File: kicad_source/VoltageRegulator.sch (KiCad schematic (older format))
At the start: 45 parts, among them CN6 691313710002, Q1 IPD90P03P4L- 04, U3 LM1085ISX-ADJ/NOPB, U9 IFX91041EJV

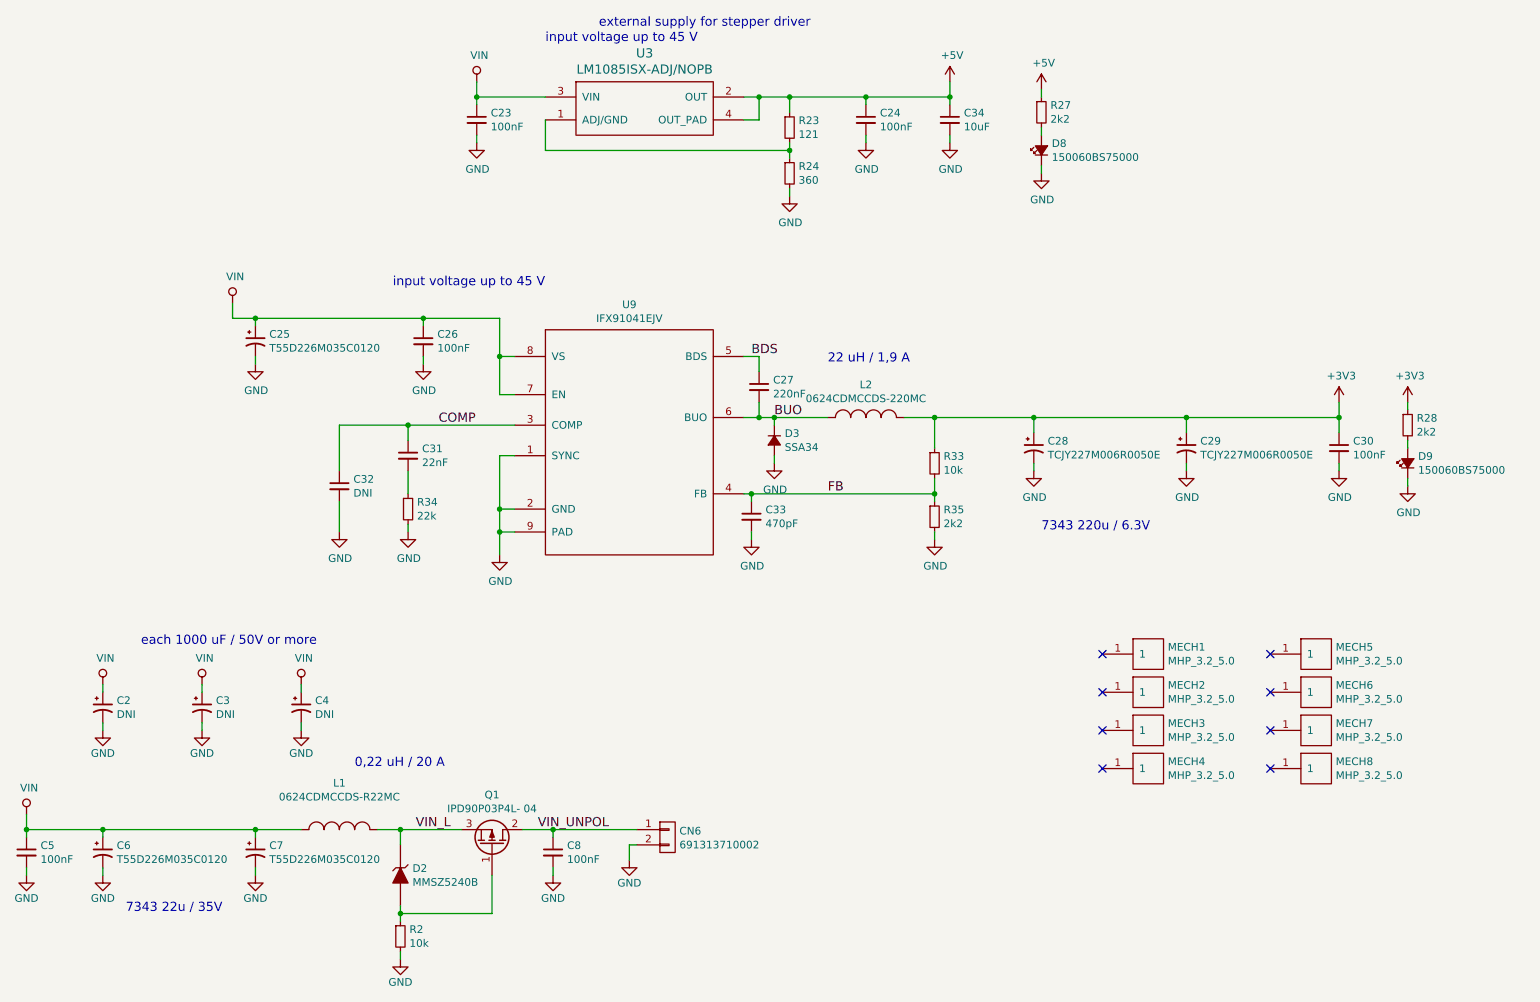
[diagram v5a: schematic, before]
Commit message: removed regulator for 5V external
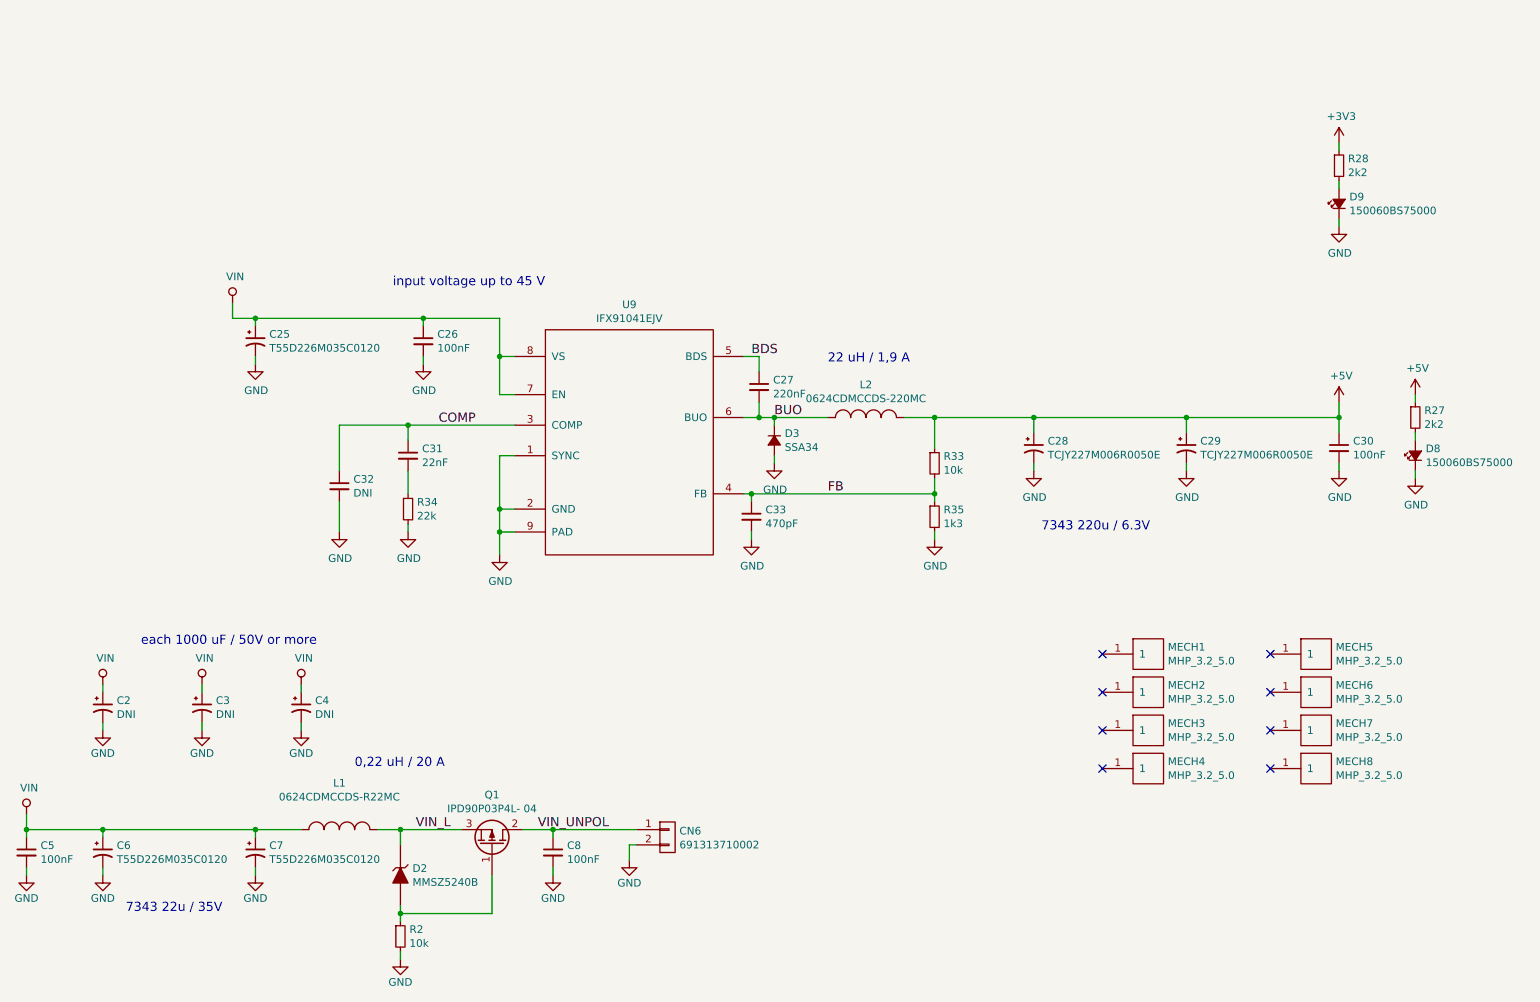
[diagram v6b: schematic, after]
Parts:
- removed C23, C24: 100nF, capacitors:C_0603, symbol devices:C_0603
- removed C34: 10uF, capacitors:C_0805, symbol devices:C_0805
- removed R23: 121, resistors:R_0603, symbol devices:R_0603
- removed R24: 360, resistors:R_0603, symbol devices:R_0603
- removed U3: LM1085ISX-ADJ/NOPB, SOT_TO:TO-263-3Lead, symbol voltage-regulators:LT1085
- R35: value 2k2 -> 1k3
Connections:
- net +3V3: no longer C28.1, C29.1, C30.1, L2.2, R33.1
- net +5V: now also C28.1, C29.1, C30.1, L2.2, R33.1
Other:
- note removed: "external supply for stepper driver"
- moved on the sheet: D8, D9, R27, R28

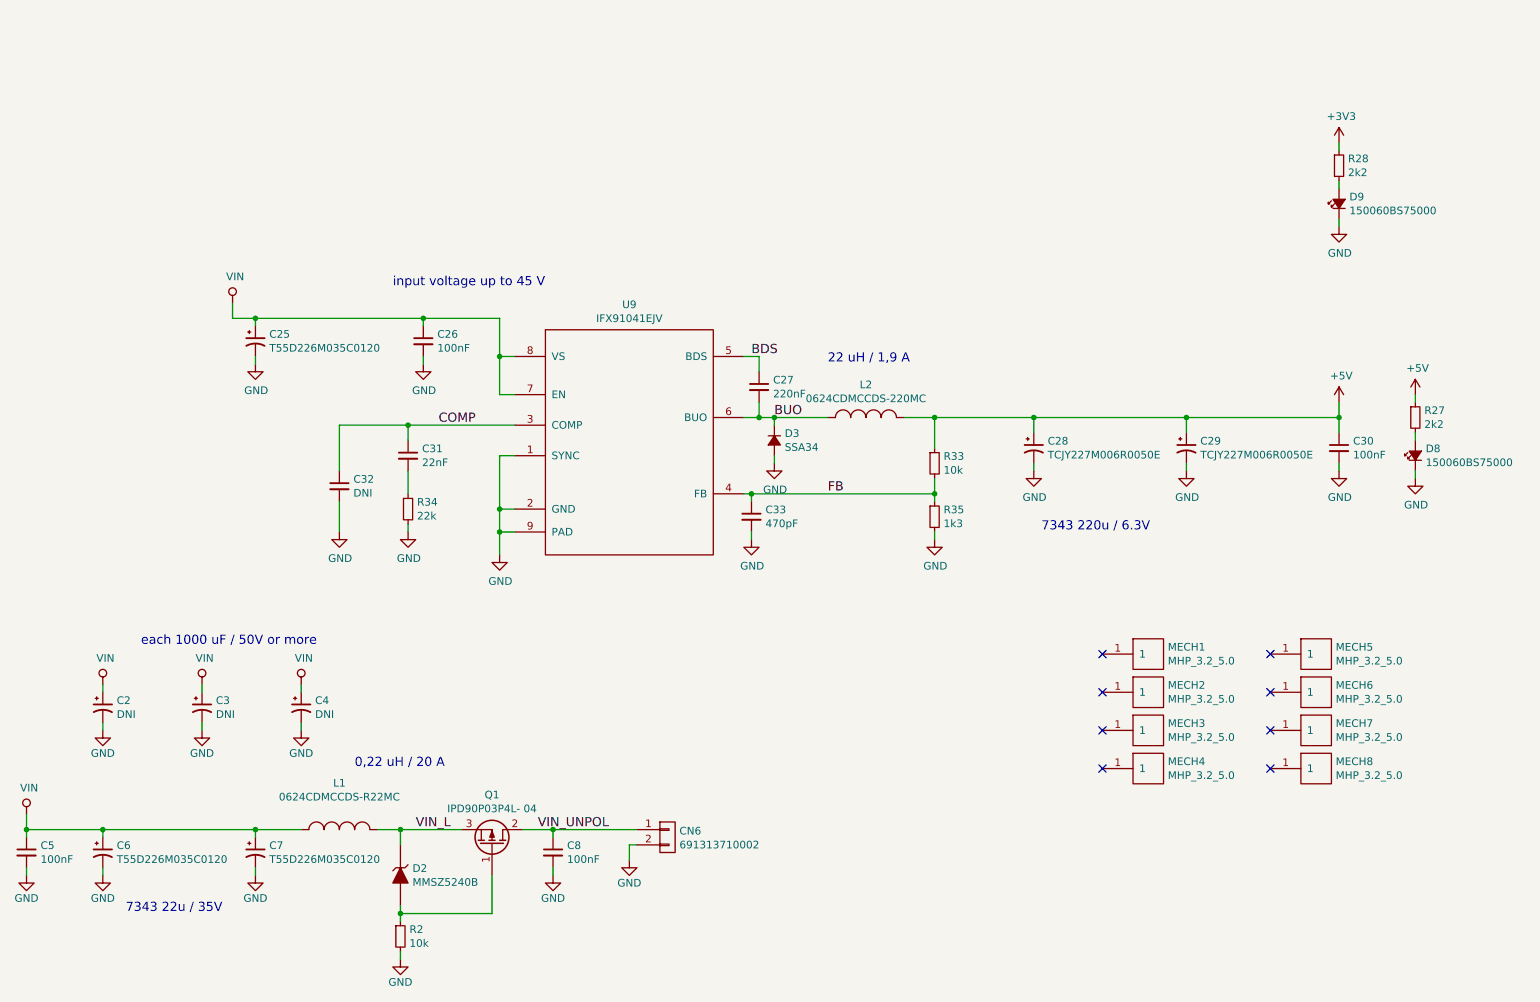
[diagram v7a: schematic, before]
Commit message: replaced tantal capacitors with aluminium-electronlytic capacitors with higher voltage to allow up to 45 V on input
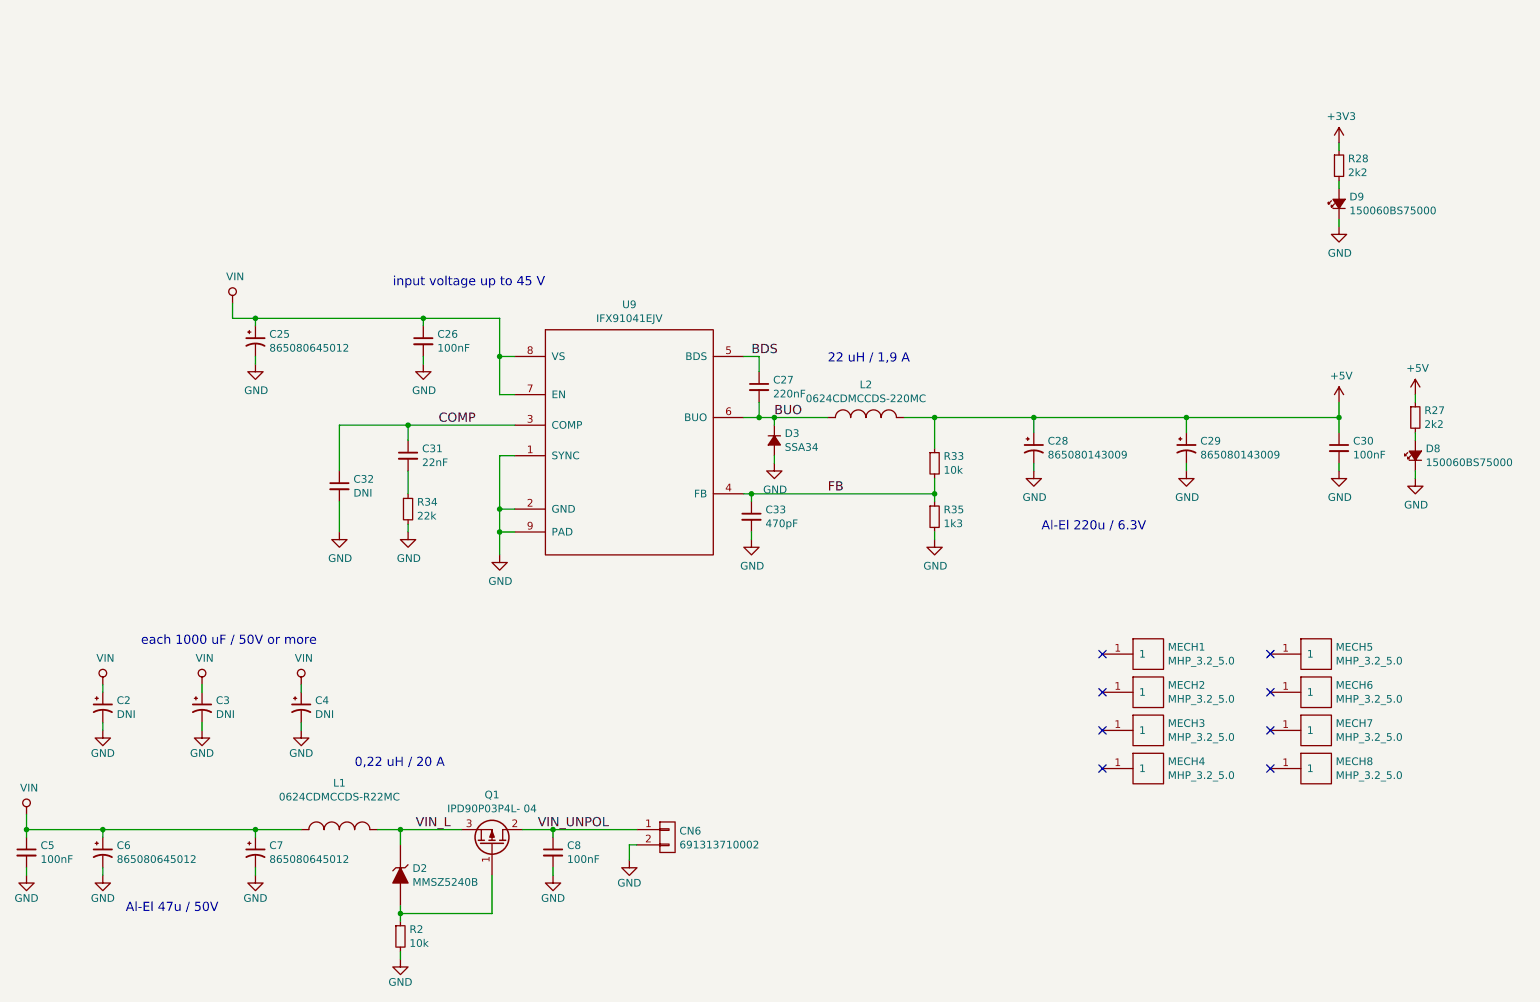
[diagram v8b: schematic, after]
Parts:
- C25, C6, C7: value T55D226M035C0120 -> 865080645012; footprint capacitors:TantalC_SizeD_EIA-7343_Wave -> capacitors:c_elec_6.3x7.7
- C28, C29: value TCJY227M006R0050E -> 865080143009; footprint capacitors:TantalC_SizeD_EIA-7343_Wave -> capacitors:c_elec_6.3x5.7
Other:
- note added: "Al-El 220u / 6.3V"
- note added: "Al-El 47u / 50V"
- note removed: "7343 220u / 6.3V"
- note removed: "7343 22u / 35V"
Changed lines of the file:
@@
 P 7800 3950
 F 0 "C28" H 7891 3996 50  0000 L CNN
-F 1 "TCJY227M006R0050E" H 7891 3905 50  0000 L CNN
-F 2 "capacitors:TantalC_SizeD_EIA-7343_Wave" H 7900 3750 50  0001 C CNN
+F 1 "865080143009" H 7891 3905 50  0000 L CNN
+F 2 "capacitors:c_elec_6.3x5.7" H 7900 3750 50  0001 C CNN
 F 3 "" H 7800 3950 50  0000 C CNN
 	1    7800 3950
@@
 P 8800 3950
 F 0 "C29" H 8891 3996 50  0000 L CNN
-F 1 "TCJY227M006R0050E" H 8891 3905 50  0000 L CNN
-F 2 "capacitors:TantalC_SizeD_EIA-7343_Wave" H 8900 3750 50  0001 C CNN
+F 1 "865080143009" H 8891 3905 50  0000 L CNN
+F 2 "capacitors:c_elec_6.3x5.7" H 8900 3750 50  0001 C CNN
 F 3 "" H 8800 3950 50  0000 C CNN
 	1    8800 3950
@@
 P 2700 3250
 F 0 "C25" H 2791 3296 50  0000 L CNN
-F 1 "T55D226M035C0120" H 2791 3205 50  0000 L CNN
-F 2 "capacitors:TantalC_SizeD_EIA-7343_Wave" H 2800 3050 50  0001 C CNN
+F 1 "865080645012" H 2791 3205 50  0000 L CNN
+F 2 "capacitors:c_elec_6.3x7.7" H 2800 3050 50  0001 C CNN
 F 3 "" H 2700 3250 50  0000 C CNN
 	1    2700 3250
@@
 AR Path="/5DE38154/5DEE0BC0" Ref="C7"  Part="1"
 F 0 "C7" H 2791 6646 50  0000 L CNN
-F 1 "T55D226M035C0120" H 2791 6555 50  0000 L CNN
-F 2 "capacitors:TantalC_SizeD_EIA-7343_Wave" H 2800 6400 50  0001 C CNN
+F 1 "865080645012" H 2791 6555 50  0000 L CNN
+F 2 "capacitors:c_elec_6.3x7.7" H 2800 6400 50  0001 C CNN
 F 3 "" H 2700 6600 50  0000 C CNN
 	1    2700 6600
@@
 AR Path="/5DE38154/5DEE0BC6" Ref="C6"  Part="1"
 F 0 "C6" H 1791 6646 50  0000 L CNN
-F 1 "T55D226M035C0120" H 1791 6555 50  0000 L CNN
-F 2 "capacitors:TantalC_SizeD_EIA-7343_Wave" H 1800 6400 50  0001 C CNN
+F 1 "865080645012" H 1791 6555 50  0000 L CNN
+F 2 "capacitors:c_elec_6.3x7.7" H 1800 6400 50  0001 C CNN
 F 3 "" H 1700 6600 50  0000 C CNN
 	1    1700 6600
@@
 each 1000 uF / 50V or more
 Text Notes 1850 7000 0    60   ~ 0
-7343 22u / 35V
+Al-El 47u / 50V
 Wire Wire Line
 	1700 6450 2700 6450
 Connection ~ 2700 6450
 Text Notes 7850 4500 0    60   ~ 0
-7343 220u / 6.3V
+Al-El 220u / 6.3V
 Wire Wire Line
 	8800 3750 9800 3750
